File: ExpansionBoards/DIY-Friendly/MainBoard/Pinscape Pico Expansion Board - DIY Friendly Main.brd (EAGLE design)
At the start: 160 x 100 mm, 114 parts, among them IC1 UCC27524P, IC10 ULN2803A, IC11 SN74HC165N, IC12 SN74HC165N, IC13 SN74HC74NE4, IC14 PC827, IC15 S-80833CLY, IC16 SN74HC165N, IC18 SN74HC165N, IC2 UCC27524P, IC3 UCC27524P, IC4 UCC27524P, IC5 UCC27524P, IC6 UCC27524P, IC7 ULN2803A, IC8 ULN2803A, IC9 ULN2803A, J1 30316-6002HB, J10 215079-4, J11 640454-2, J13 640445-2, J2 640445-4, J3 640445-5, J4 640445-9, J5 1-640456-0, J6 1-640456-0, J7 1-640456-0, J8 1-640456-0, J9 30308-6002HB, Q1 FDPF085N10A, Q10 FDPF085N10A, Q11 FDPF085N10A, Q12 FDPF085N10A, Q13 BC337-25, Q15 2N5195G, Q16 2N2222A, Q2 FDPF085N10A, Q3 FDPF085N10A, Q4 FDPF085N10A, Q5 FDPF085N10A, Q6 FDPF085N10A, Q7 FDPF085N10A, Q8 FDPF085N10A, Q9 FDPF085N10A

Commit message: expansion board improvements
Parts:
- J2: value 640445-4 -> 640445-6; device SamacSys_Parts:SHDR4W117P0X396_1X4_1585X762X1 -> SamacSys_Parts:SHDR6W183P0X396_1X6_2377X762X1
- moved J2 12.2 mm to (96.3, 95.9), turned to 0 degrees
- moved J4 4.24 mm to (51.6, 96.0)
- moved J3 3.78 mm to (83.5, 95.9)
- moved J1 1.90 mm to (134.1, 92.9)
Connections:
- net 12V: now also J2.5; no longer J2.3
- net 5V: now also J2.6; no longer J2.4
- net GND: now also J2.3, J2.4
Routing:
- net OUT6: track 17.2 -> 22.7 mm
- net OUT5: track 15.8 -> 21.1 mm
- net OUT12: track 25.1 -> 30.3 mm
- net OUT10: track 20.5 -> 25.5 mm
- net OUT8: track 21.7 -> 26.3 mm
- net OUT7: track 19.8 -> 24.1 mm
- net OUT4: track 15.2 -> 19.2 mm
- net OUT11: track 23.4 -> 27.4 mm
- net OUT9: track 22.0 -> 25.8 mm
- net 5V: track 329.5 -> 325.8 mm
- net 12V: track 187.5 -> 190.5 mm
- net FLASHER15: track 26.4 -> 24.3 mm
- net FLASHER14: track 33.6 -> 31.8 mm
- net FLASHER6: track 50.2 -> 51.9 mm
- net FLASHER13: track 40.0 -> 38.3 mm
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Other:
- board text added: "DIY MAIN BOARD 20250106"
- board text removed: "DIY MAIN BOARD 20241215"

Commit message: add logo image
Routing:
- net GND: track 0.00 -> 17.6 mm
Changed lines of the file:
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@@
 <contactref element="D4" pad="C"/>
 <contactref element="R31" pad="1"/>
-<polygon width="1" layer="1" thermals="no">
-<vertex x="94.8" y="93.3"/>
-<vertex x="110.1" y="93.3"/>
-<vertex x="110.1" y="98"/>
-<vertex x="94.8" y="98"/>
-</polygon>
-<polygon width="1" layer="16" thermals="no">
-<vertex x="94.9" y="93.3"/>
-<vertex x="110.1" y="93.3"/>
-<vertex x="110.1" y="98"/>
-<vertex x="94.9" y="98"/>
-</polygon>
 <contactref element="J2" pad="1"/>
 <contactref element="J2" pad="2"/>
@@
 <vertex x="147.2" y="61.5"/>
 </polygon>
+<wire x1="96.3" y1="95.9" x2="96.3" y2="93.7" width="1.5" layer="16"/>
+<wire x1="100.26" y1="95.9" x2="100.26" y2="93.64" width="1.5" layer="16"/>
+<wire x1="104.22" y1="95.9" x2="104.22" y2="93.68" width="1.5" layer="16"/>
+<wire x1="108.18" y1="95.9" x2="108.18" y2="93.62" width="1.5" layer="16"/>
+<wire x1="96.3" y1="95.9" x2="96.3" y2="98" width="1.5" layer="1"/>
+<wire x1="100.26" y1="95.9" x2="100.26" y2="93.84" width="1.5" layer="1"/>
+<wire x1="104.22" y1="95.9" x2="104.22" y2="93.72" width="1.5" layer="1"/>
+<wire x1="108.18" y1="95.9" x2="108.2" y2="93.6" width="1.5" layer="1"/>
 </signal>
 <signal name="SDA">
@@
 <wire x1="109.3" y1="69.4" x2="109.3" y2="82.8" width="1" layer="16"/>
 <wire x1="107.93" y1="68.03" x2="107.3" y2="68.03" width="1" layer="16"/>
-<wire x1="110.284" y1="83.784" x2="109.6" y2="83.1" width="1" layer="16"/>
 <contactref element="J2" pad="5"/>
-<wire x1="109.6" y1="83.1" x2="109.3" y2="82.8" width="1" layer="16"/>
 <wire x1="112.14" y1="95.9" x2="112.14" y2="85.64" width="1" layer="16"/>
-<wire x1="112.14" y1="85.64" x2="110.284" y2="83.784" width="1" layer="16"/>
+<wire x1="112.14" y1="85.64" x2="109.3" y2="82.8" width="1" layer="16"/>
 </signal>
 <signal name="OUTCTL2">

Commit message: minor board updates
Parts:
- R26, R28, R32, R33: device resistor:0204/5 -> resistor:0204/7
- moved R26 1.30 mm to (96.7, 49.0)
- moved R32 1.21 mm to (113.1, 43.3)
- moved R28 1.20 mm to (96.7, 46.5)
- moved R33 1.10 mm to (115.8, 43.3)
- moved Q16 0.80 mm to (104.9, 43.7)
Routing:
- net GND: track 17.6 -> 39.1 mm
- net N$24: track 6.17 -> 8.75 mm
- net 3V3_PICO: track 374.2 -> 375.8 mm
- net /AUX_RESET: track 66.9 -> 67.6 mm

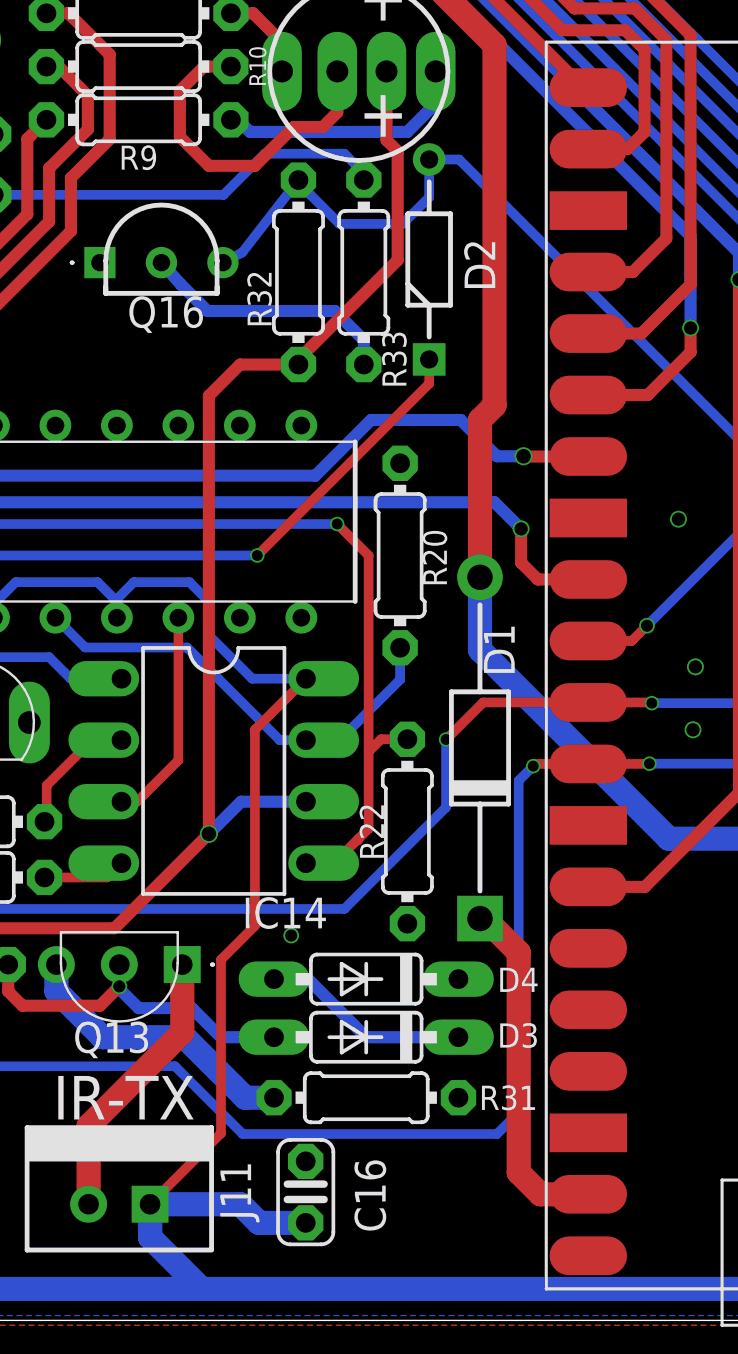
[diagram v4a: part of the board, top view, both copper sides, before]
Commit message: Remove pull-up to primary Pico 3V3 on aux Pico reset
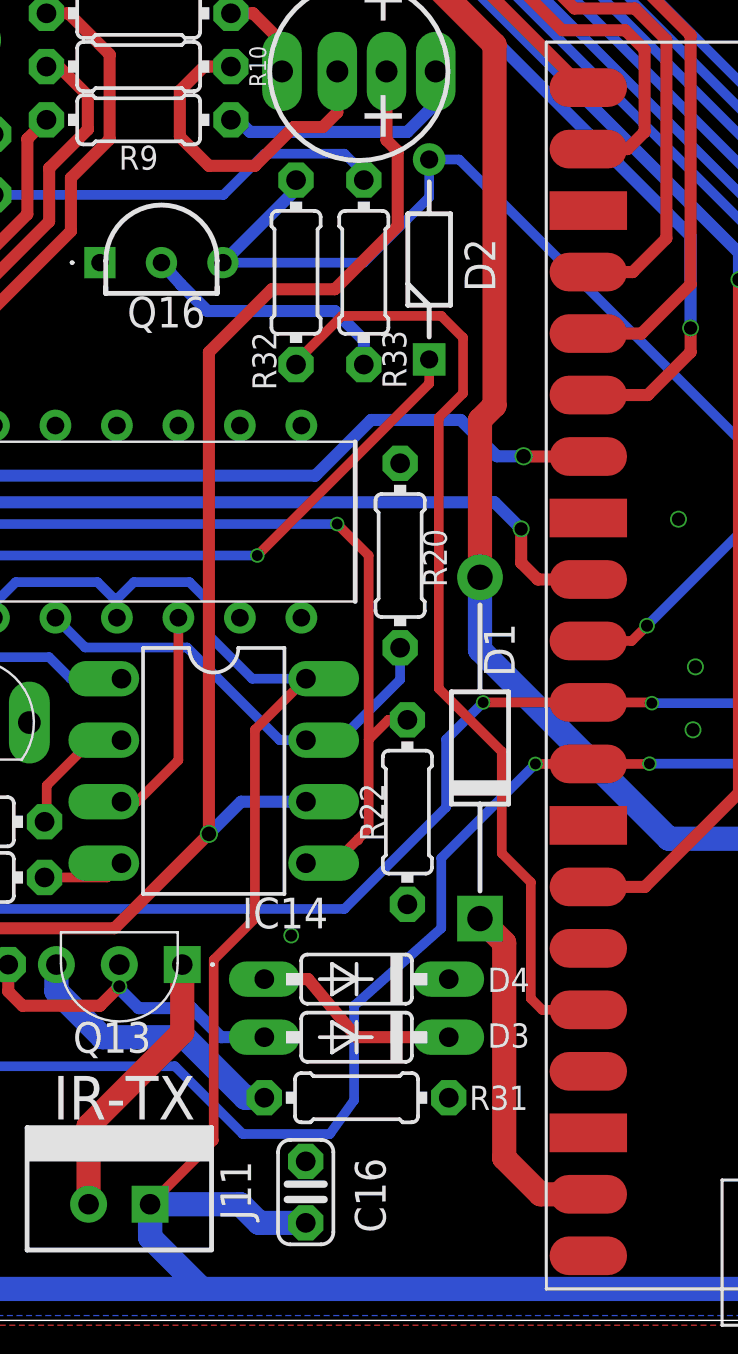
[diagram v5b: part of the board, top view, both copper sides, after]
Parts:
- R32: value 10K -> 2.2K
- moved R22 0.80 mm to (117.6, 21.0)
- moved D3 0.40 mm to (115.5, 11.7)
- moved D4 0.40 mm to (115.5, 14.1)
- moved R31 0.40 mm to (115.5, 9.20)
- moved R32 0.10 mm to (113.0, 43.3)
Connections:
- new net N$34: PICO2.3V3, R32.2
- net 3V3_PICO: no longer R32.2
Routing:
- net N$34: track 0.00 -> 40.0 mm
- net SCL: track 183.6 -> 179.6 mm
- net /AUX_RESET: track 67.6 -> 70.5 mm

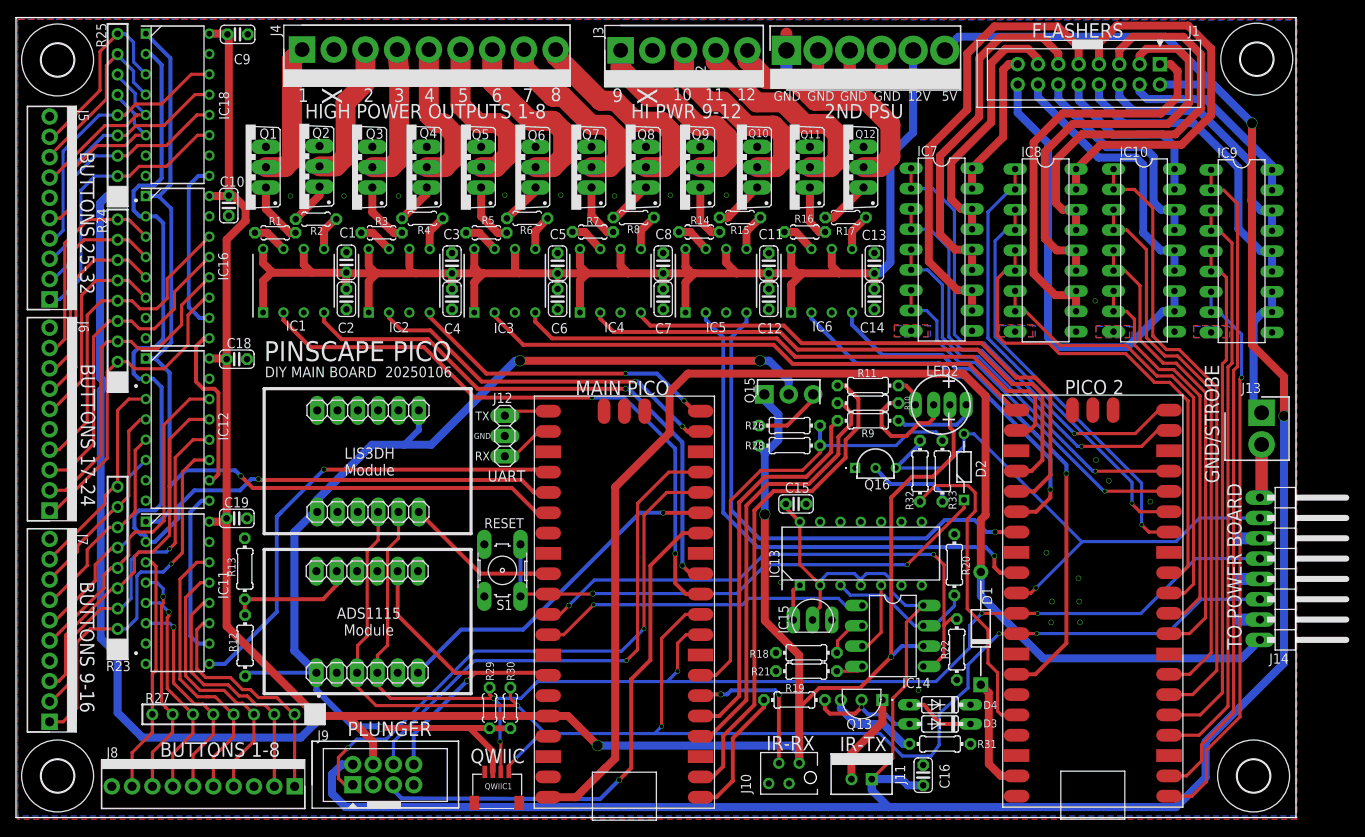
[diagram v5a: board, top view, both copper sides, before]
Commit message: DIY board: individual reset buttons per Pico; swap cross-board connectors
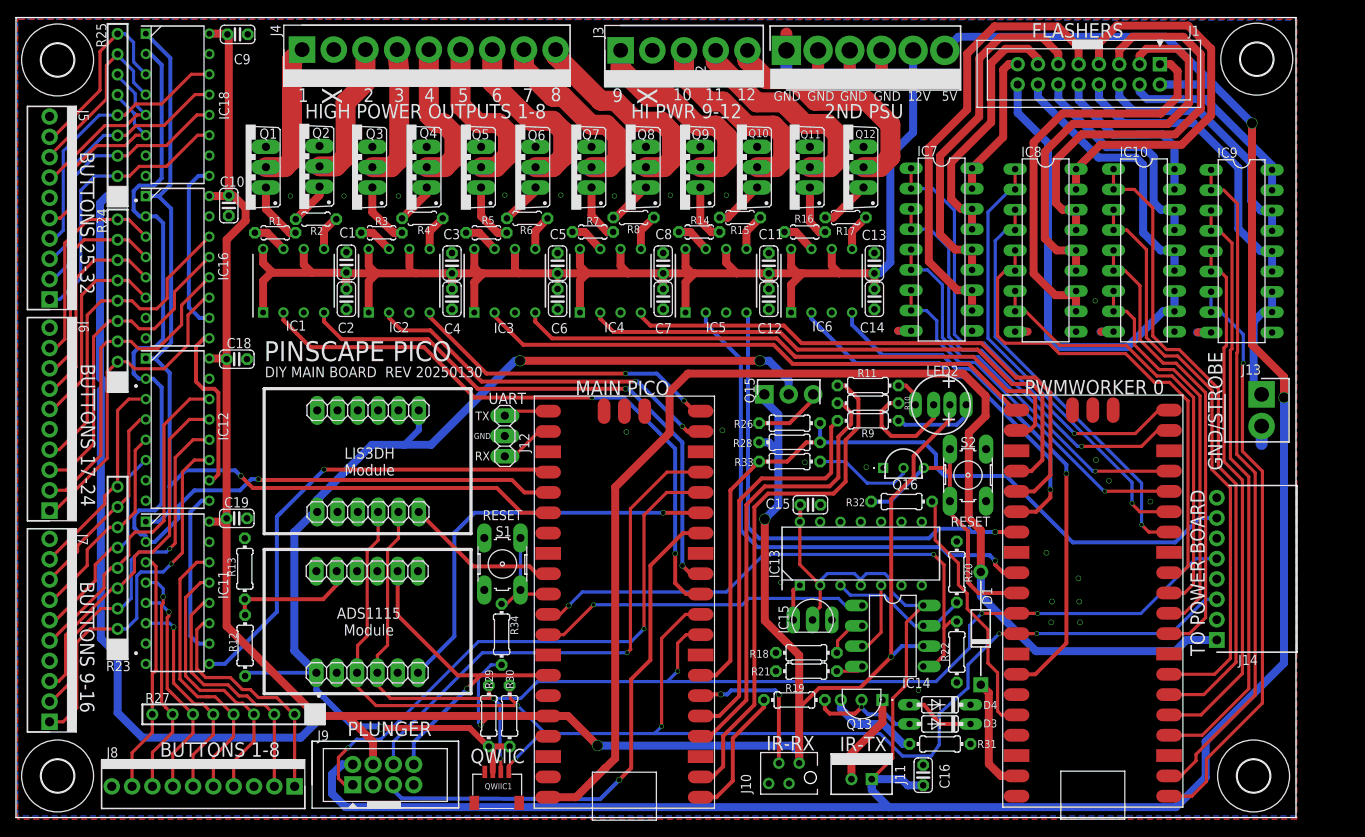
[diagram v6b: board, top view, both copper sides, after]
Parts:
- removed D2: 1N5711, SamacSys_Parts:DIOAD1084W56L378D176
- added R34: 4.7K, resistor:0204/7
- added S2: (no value), switch-omron:B3F-10XX
- J14: value (none) -> SSQ-108-02-T-S-RA; device pinhead:1X08/90 -> SamacSys_Parts:RHDRRA8W64P254_1X8_2083X851X24
- R29, R30: device resistor:0204/5 -> resistor:0204/7
- R32: value 2.2K -> 4.7K
- moved R33 19.1 mm to (96.7, 44.5), turned to 0 degrees
- moved J14 12.8 mm to (150.1, 22.2)
- moved R32 4.44 mm to (110.7, 39.5), turned to 0 degrees
- moved Q16 3.50 mm to (108.4, 43.7)
- moved J13 2.30 mm to (155.7, 52.9)
- moved C15 1.80 mm to (99.3, 39.1)
- moved R29 1.00 mm to (59.1, 12.7)
- moved R30 1.00 mm to (61.7, 12.7)
- moved R20 0.95 mm to (117.6, 30.7)
- moved S1 0.80 mm to (60.8, 31.7)
- moved R28 0.40 mm to (96.7, 46.9)
- moved R22 0.30 mm to (117.6, 20.7)
- moved R26 0.30 mm to (96.7, 49.3)
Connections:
- removed net /AUX_RESET: D2.2, J14.2, PICO2.RUN, Q16.3, R32.1
- removed net /RESET: D2.1, PICO1.RUN, S1.3, S1.4
- new net N$35: PICO2.RUN, Q16.3, R32.1, S2.3, S2.4
- new net N$36: PICO1.RUN, R34.1, S1.3, S1.4
- net /PERIPHERAL_POWER_ENABLE: now also J14.7
- net 3V3_PICO: now also R34.2
- net GND: now also J14.2, J14.4, J14.6, J14.8, S2.1, S2.2; no longer J14.1, J14.3, J14.5, J14.7
- net SCL: now also J14.3; no longer J14.6
- net SDA: now also J14.5; no longer J14.4
- net VBUS: now also J14.1; no longer J14.8
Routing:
- net /AUX_RESET: track 70.5 -> 0.00 mm, vias 1 -> 0
- net /RESET: track 67.9 -> 0.00 mm, vias 2 -> 0
- net /PERIPHERAL_POWER_ENABLE: track 58.2 -> 98.9 mm
- net N$35: track 0.00 -> 36.2 mm
- net N$36: track 0.00 -> 13.3 mm
- net 3V3_PICO: track 375.9 -> 387.1 mm, vias 3 -> 4
- net N$34: track 40.0 -> 32.2 mm
- net ADC_INTR: track 43.6 -> 51.2 mm
- net GND: track 39.1 -> 32.7 mm, vias 20 -> 24
- net SCL: track 179.6 -> 174.4 mm
- net SDA: track 163.7 -> 158.6 mm
- net VBUS: track 164.9 -> 160.0 mm
- net FLASHCTL11: track 68.7 -> 72.5 mm
- net FLASHCTL12: track 77.7 -> 80.5 mm
- net OUTCTL10: track 64.2 -> 61.7 mm
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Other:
- board text added: "DIY MAIN BOARD REV 20250130"
- board text added: "PWMWORKER 0"
- board text removed: "DIY MAIN BOARD 20250106"
- board text removed: "PICO 2"
